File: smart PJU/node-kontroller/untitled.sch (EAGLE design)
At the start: 48 parts, among them J1 U.FL-R-SMT(01), J2 10118193-0001LF, K1 351, Q1 S9013, Q16 MMBT3904, Q17 MMBT3904, Q18 12MHz, U1 AMS1117, U19 CH340G, U2 PC817X2NIP0F

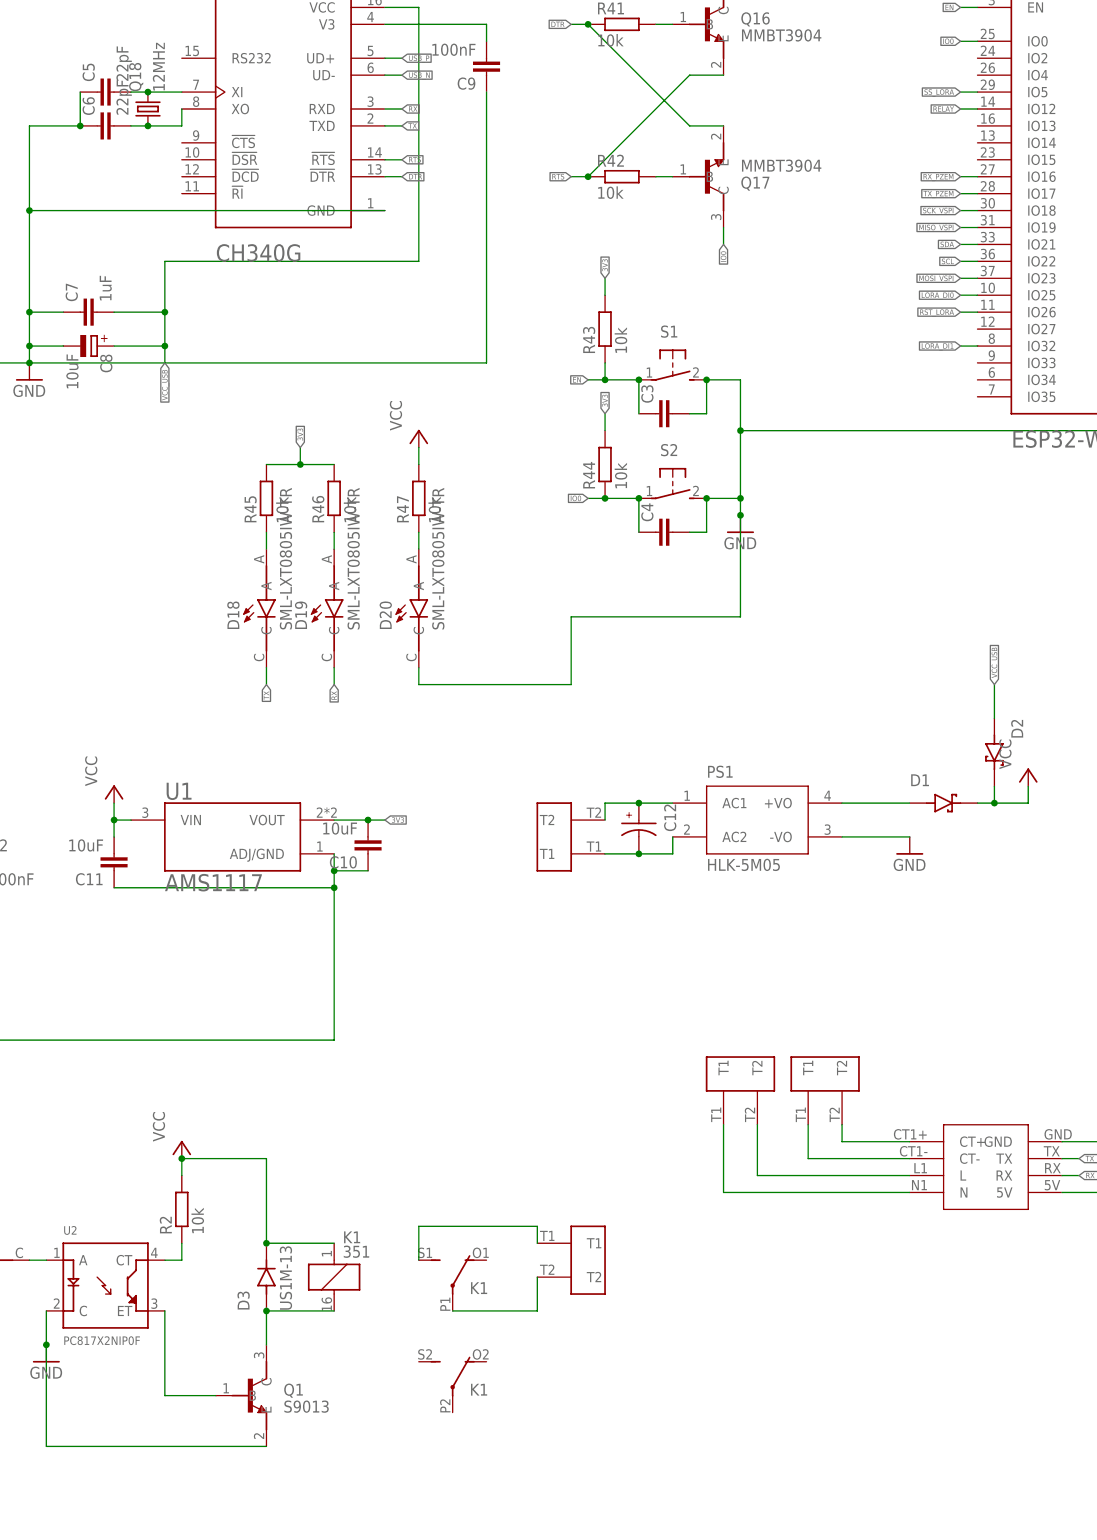
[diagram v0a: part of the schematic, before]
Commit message: revisi relay node dan list komponen
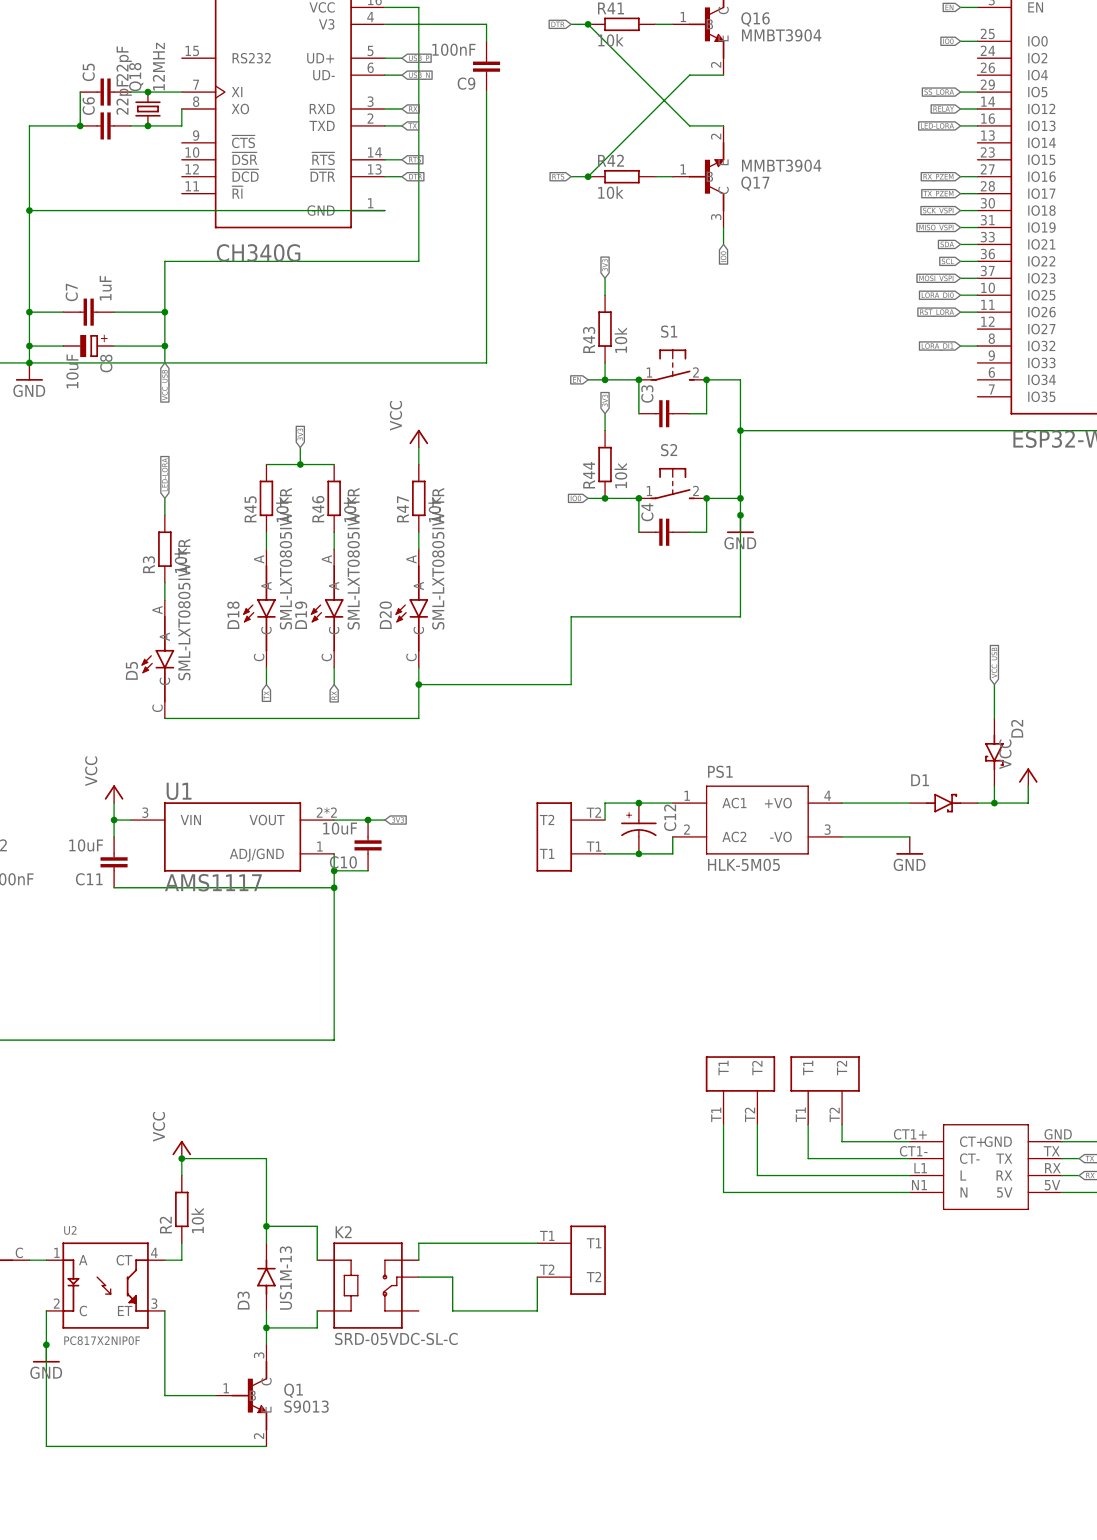
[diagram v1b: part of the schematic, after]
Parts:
- removed K1: 351, relay:351
- added D5: SML-LXT0805IW-TR, SML-LXT0805IW-TR:SML-LXT0805IW-TR
- added K2: SRD-05VDC-SL-C, SRD-05VDC-SL-C:SRD-05VDC-SL-C
- added R3: 10k, rcl:R-EU_R0805
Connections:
- new net LED-LORA: MD1.IO13, R3.2
- new net N$12: D5.A, R3.1
- net GND: now also D5.C
- net N$10: now also K2.NO; no longer K12.S
- net N$7: now also K2.A2; no longer K11.2
- net N$9: now also K2.COM; no longer K12.P
- net VCC: now also K2.A1; no longer K11.1
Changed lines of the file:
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@@
 <part name="R2" library="rcl" library_urn="urn:adsk.eagle:library:334" deviceset="R-EU_" device="R0805" package3d_urn="urn:adsk.eagle:package:23553/2" value="10k"/>
 <part name="D3" library="US1M-13" deviceset="US1M-13" device=""/>
-<part name="K1" library="relay" library_urn="urn:adsk.eagle:library:339" deviceset="351" device="" package3d_urn="urn:adsk.eagle:package:24300/1"/>
 <part name="Q1" library="S9013" deviceset="S9013" device=""/>
 <part name="GND5" library="supply1" library_urn="urn:adsk.eagle:library:371" deviceset="GND" device=""/>
@@
 <part name="TB7.3" library="TB7.62" deviceset="TB7.62" device=""/>
 <part name="TB7.4" library="TB7.62" deviceset="TB7.62" device=""/>
+<part name="K2" library="SRD-05VDC-SL-C" deviceset="SRD-05VDC-SL-C" device=""/>
+<part name="D5" library="SML-LXT0805IW-TR" deviceset="SML-LXT0805IW-TR" device=""/>
+<part name="R3" library="rcl" library_urn="urn:adsk.eagle:library:334" deviceset="R-EU_" device="R0805" package3d_urn="urn:adsk.eagle:package:23553/2" value="10k"/>
 </parts>
 <sheets>
@@
 <attribute name="VALUE" x="90.17" y="182.88" size="1.778" layer="96" rot="R90"/>
 </instance>
-<instance part="K1" gate="1" x="96.52" y="187.96" smashed="yes">
-<attribute name="VALUE" x="97.79" y="190.881" size="1.778" layer="96"/>
-<attribute name="PART" x="97.79" y="193.04" size="1.778" layer="95"/>
-</instance>
-<instance part="K1" gate="2" x="114.3" y="185.42" smashed="yes">
-<attribute name="PART" x="116.84" y="185.42" size="1.778" layer="95"/>
-</instance>
-<instance part="K1" gate="3" x="114.3" y="170.18" smashed="yes">
-<attribute name="PART" x="116.84" y="170.18" size="1.778" layer="95"/>
-</instance>
 <instance part="Q1" gate="G$1" x="83.82" y="170.18" smashed="yes">
 <attribute name="NAME" x="88.90085" y="170.18" size="1.7783" layer="95"/>
@@
 <instance part="TB7.3" gate="G$1" x="170.18" y="218.44" smashed="yes"/>
 <instance part="TB7.4" gate="G$1" x="157.48" y="218.44" smashed="yes"/>
+<instance part="K2" gate="G$1" x="101.6" y="187.96" smashed="yes">
+<attribute name="NAME" x="96.5191" y="193.803040625" size="1.77831875" layer="95"/>
+<attribute name="VALUE" x="96.516809375" y="177.7936" size="1.77911875" layer="96"/>
+</instance>
+<instance part="D5" gate="G$1" x="71.12" y="279.4" smashed="yes" rot="R90">
+<attribute name="NAME" x="67.04973125" y="277.36486875" size="1.780740625" layer="95" rot="R90"/>
+<attribute name="VALUE" x="74.93315" y="277.36631875" size="1.77946875" layer="96" rot="R90"/>
+</instance>
+<instance part="R3" gate="G$1" x="71.12" y="297.18" smashed="yes" rot="R90">
+<attribute name="NAME" x="69.6214" y="293.37" size="1.778" layer="95" rot="R90"/>
+<attribute name="VALUE" x="74.422" y="293.37" size="1.778" layer="96" rot="R90"/>
+</instance>
 </instances>
 <busses>
@@
 <segment>
 <pinref part="D3" gate="G$1" pin="K"/>
-<wire x1="86.36" y1="193.04" x2="86.36" y2="205.74" width="0.1524" layer="91"/>
+<wire x1="86.36" y1="193.04" x2="86.36" y2="195.58" width="0.1524" layer="91"/>
+<wire x1="86.36" y1="195.58" x2="86.36" y2="205.74" width="0.1524" layer="91"/>
 <wire x1="86.36" y1="205.74" x2="73.66" y2="205.74" width="0.1524" layer="91"/>
 <pinref part="R2" gate="G$1" pin="2"/>
 <wire x1="73.66" y1="205.74" x2="73.66" y2="203.2" width="0.1524" layer="91"/>
-<pinref part="K1" gate="1" pin="1"/>
-<wire x1="96.52" y1="193.04" x2="86.36" y2="193.04" width="0.1524" layer="91"/>
-<junction x="86.36" y="193.04"/>
 <pinref part="P+4" gate="VCC" pin="VCC"/>
 <junction x="73.66" y="205.74"/>
+<pinref part="K2" gate="G$1" pin="A1"/>
+<wire x1="93.98" y1="190.5" x2="93.98" y2="195.58" width="0.1524" layer="91"/>
+<wire x1="93.98" y1="195.58" x2="86.36" y2="195.58" width="0.1524" layer="91"/>
+<junction x="86.36" y="195.58"/>
 </segment>
 <segment>
@@
 <wire x1="132.08" y1="276.86" x2="109.22" y2="276.86" width="0.1524" layer="91"/>
 <wire x1="109.22" y1="276.86" x2="109.22" y2="279.4" width="0.1524" layer="91"/>
+<pinref part="D5" gate="G$1" pin="C"/>
+<wire x1="71.12" y1="271.78" x2="109.22" y2="271.78" width="0.1524" layer="91"/>
+<wire x1="109.22" y1="271.78" x2="109.22" y2="276.86" width="0.1524" layer="91"/>
+<junction x="109.22" y="276.86"/>
 </segment>
 <segment>
@@
 <pinref part="D3" gate="G$1" pin="A"/>
 <pinref part="Q1" gate="G$1" pin="C"/>
-<wire x1="86.36" y1="182.88" x2="86.36" y2="177.8" width="0.1524" layer="91"/>
-<pinref part="K1" gate="1" pin="2"/>
-<wire x1="96.52" y1="182.88" x2="86.36" y2="182.88" width="0.1524" layer="91"/>
-<junction x="86.36" y="182.88"/>
+<wire x1="86.36" y1="182.88" x2="86.36" y2="180.34" width="0.1524" layer="91"/>
+<pinref part="K2" gate="G$1" pin="A2"/>
+<wire x1="86.36" y1="180.34" x2="86.36" y2="177.8" width="0.1524" layer="91"/>
+<wire x1="93.98" y1="182.88" x2="93.98" y2="180.34" width="0.1524" layer="91"/>
+<wire x1="93.98" y1="180.34" x2="86.36" y2="180.34" width="0.1524" layer="91"/>
+<junction x="86.36" y="180.34"/>
 </segment>
 </net>
@@
 <net name="N$9" class="0">
 <segment>
-<pinref part="K1" gate="2" pin="P"/>
-<wire x1="114.3" y1="182.88" x2="127" y2="182.88" width="0.1524" layer="91"/>
 <pinref part="TB7.2" gate="G$1" pin="T2"/>
 <wire x1="127" y1="187.96" x2="127" y2="182.88" width="0.1524" layer="91"/>
-</segment>
-</net>
-<net name="N$10" class="0">
-<segment>
-<pinref part="K1" gate="2" pin="S"/>
-<wire x1="109.22" y1="190.5" x2="109.22" y2="195.58" width="0.1524" layer="91"/>
-<wire x1="109.22" y1="195.58" x2="127" y2="195.58" width="0.1524" layer="91"/>
-<pinref part="TB7.2" gate="G$1" pin="T1"/>
-<wire x1="127" y1="193.04" x2="127" y2="195.58" width="0.1524" layer="91"/>
+<wire x1="127" y1="182.88" x2="114.3" y2="182.88" width="0.1524" layer="91"/>
+<wire x1="114.3" y1="182.88" x2="114.3" y2="187.96" width="0.1524" layer="91"/>
+<pinref part="K2" gate="G$1" pin="COM"/>
+<wire x1="114.3" y1="187.96" x2="109.22" y2="187.96" width="0.1524" layer="91"/>
 </segment>
 </net>
@@
 </segment>
 </net>
+<net name="N$10" class="0">
+<segment>
+<pinref part="TB7.2" gate="G$1" pin="T1"/>
+<pinref part="K2" gate="G$1" pin="NO"/>
+<wire x1="127" y1="193.04" x2="109.22" y2="193.04" width="0.1524" layer="91"/>
+<wire x1="109.22" y1="193.04" x2="109.22" y2="190.5" width="0.1524" layer="91"/>
+</segment>
+</net>
+<net name="N$12" class="0">
+<segment>
+<pinref part="D5" gate="G$1" pin="A"/>
+<pinref part="R3" gate="G$1" pin="1"/>
+<wire x1="71.12" y1="289.56" x2="71.12" y2="292.1" width="0.1524" layer="91"/>
+</segment>
+</net>
+<net name="LED-LORA" class="0">
+<segment>
+<pinref part="MD1" gate="G$0" pin="IO13"/>
+<wire x1="193.04" y1="360.68" x2="190.5" y2="360.68" width="0.1524" layer="91"/>
+<label x="190.5" y="360.68" size="0.8128" layer="95" rot="R180" xref="yes"/>
+</segment>
+<segment>
+<pinref part="R3" gate="G$1" pin="2"/>
+<wire x1="71.12" y1="302.26" x2="71.12" y2="304.8" width="0.1524" layer="91"/>
+<label x="71.12" y="304.8" size="0.8128" layer="95" rot="R90" xref="yes"/>
+</segment>
+</net>
